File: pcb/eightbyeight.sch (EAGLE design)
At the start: 140 parts, among them CON1 USB_MICROSMT+THRUHULE, Q1 16MHz, SW1 SWITCH_SPDT, SW2 BRIGHTNESS, U1 MK20DN64VFM5, U10 FDG6316P, U11 FDG6316P, U12 FDG6316P, U2 ICN2026, U3 74138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

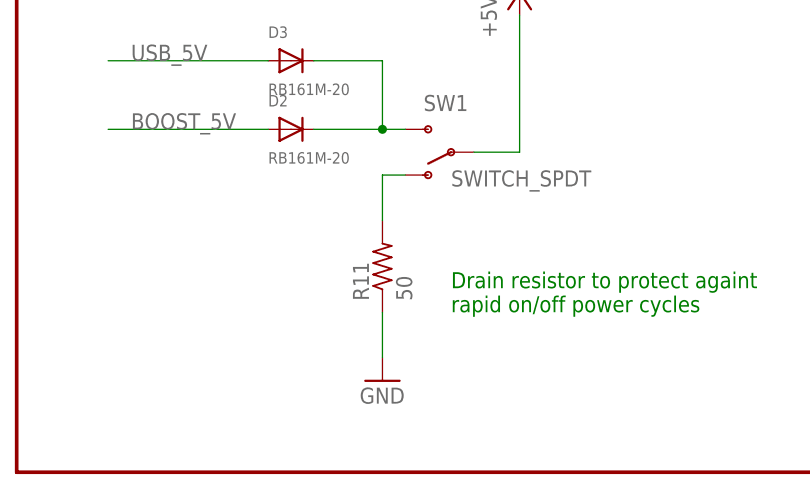
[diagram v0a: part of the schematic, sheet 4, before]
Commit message: Update board TODOs
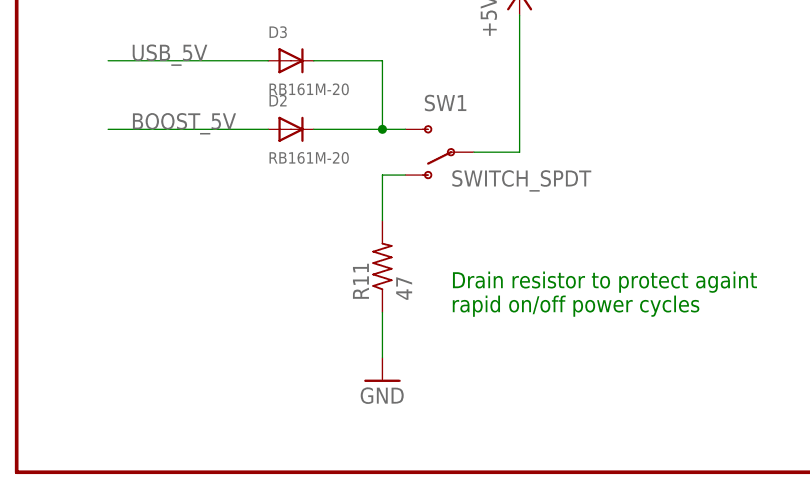
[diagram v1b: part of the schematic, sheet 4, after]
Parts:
- R11: value 50 -> 47
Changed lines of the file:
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@@
 <part name="D2" library="adafruit" deviceset="DIODE" device="SOD-123" value="RB161M-20"/>
 <part name="D3" library="adafruit" deviceset="DIODE" device="SOD-123" value="RB161M-20"/>
-<part name="R11" library="adafruit" deviceset="R-US_" device="R0805" value="50"/>
+<part name="R11" library="adafruit" deviceset="R-US_" device="R0805" value="47"/>
 <part name="GND43" library="SparkFun-Aesthetics" deviceset="GND" device=""/>
 <part name="16" library="testpad" deviceset="PTR1" device="B2,54"/>

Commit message: Silkscreen tweaks to pcbs
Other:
- note added: "High side (row) drivers"
- note removed: "High side (column) drivers"
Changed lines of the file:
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@@
 <wire x1="7.62" y1="101.6" x2="276.86" y2="101.6" width="0.4064" layer="94"/>
 <text x="12.7" y="71.12" size="1.778" layer="91">P channel MOSFETs with gate drive capability</text>
-<text x="12.7" y="76.2" size="2.54" layer="94">High side (column) drivers</text>
+<text x="12.7" y="76.2" size="2.54" layer="94">High side (row) drivers</text>
 <wire x1="7.62" y1="83.82" x2="274.32" y2="83.82" width="0.4064" layer="94"/>
 <wire x1="7.62" y1="7.62" x2="7.62" y2="83.82" width="0.4064" layer="94"/>

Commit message: Test pads in progress
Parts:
- removed U$2: JTAG_ARM_10PIN, blinkinlabs:JTAG_ARM_10PIN
- added R22: 100, adafruit:R-US_R0402
- added TP1, TP10, TP11, TP12, TP13, TP14, TP15, TP17, TP18, TP19, TP2, TP20, TP21, TP22, TP23, TP24, TP3, TP4, TP5, TP6, TP7, TP8, TP9: PTR1B1,27, testpad:PTR1B1,27
- C16: value 470pF -> 47pF
- D1: value BLUE -> ORANGE
- D4: value BLUE -> PURPLE
- R12, R23, R25, R26, R27, R6: value 10k -> 47k
- R21: value 2k 1% -> 47k
- R28: value 10k -> DNP
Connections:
- new net N$1: D1.C, D4.C, R22.2
- net +5V: now also TP7.TP
- net ARM_3V3: now also TP9.TP; no longer U$2.VCC
- net ARM_RESET: now also TP14.TP; no longer U$2.RESET
- net ARM_RX: now also TP13.TP; no longer U$2.TDI
- net ARM_RX1: now also TP23.TP
- net ARM_TCK: now also TP11.TP; no longer U$2.TCK
- net ARM_TMS: now also TP10.TP; no longer U$2.TMS
- net ARM_TX: now also TP12.TP; no longer U$2.TDO
- net BOOST_5V: now also TP24.TP
- net ESP_GPIO0: now also TP15.TP
- net ESP_RESET: now also TP17.TP
- net GND: now also R22.1, TP18.TP; no longer D1.C, D4.C, U$2.GND
- net I2C_SCL: now also TP6.TP
- net I2C_SDA: now also TP5.TP
- net LED_CLK: now also TP2.TP
- net LED_DAT_0: now also TP1.TP
- net LED_HS_EN: now also TP22.TP
- net LED_OE: now also TP4.TP
- net LED_ROW_A: now also TP19.TP
- net LED_ROW_B: now also TP20.TP
- net LED_ROW_C: now also TP21.TP
- net LED_STB: now also TP3.TP
- net VBAT: now also TP8.TP
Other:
- note added: "ESP test pins"
- note added: "JTAG interface for ARM"
- note added: "LED Test points"
- note added: "Momentary, active low Connected to ESP"
- note added: "Note: The I2C bus runs at 100KHz"
- note added: "Pin assignments for matrix output: LED_DAT + LED_CLK use ESPI hardware LED_OE needs to be on a pin with FTM capability LED_ROW_* and LED_STB are GPIO and need to be together on a unique port"
- note added: "Power supply Test points"
- note added: "Used during automated production testing Note: RX and TX are available on the ARM JTAG pins"
- note added: "Used for automated production testing"
- note removed: "ARM 10pin JTAG/SWD"
- note removed: "Momentary, active low Connected to ESP and ARM"
- note removed: "Note: Check that these values are correct for 3.3V"
- note removed: "Pin assignments for matrix output: LED_DAT + LED_CLK need to be together on a unique port LED_ROW_* and LED_STB need to be together on a unique port LED_OE needs to be on a pin with FTM capability"

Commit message: Closer to RevD
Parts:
- removed L2: 130ohm @100MHz, blinkinlabs:FB0805/NO-OUTLINE
- removed R22: 100, adafruit:R-US_R0402
- added SJ1: SOLDERJUMPERTRACE, SparkFun-Passives:SOLDERJUMPERTRACE
- added TP25: PTR1B1,27, testpad:PTR1B1,27
- added Z3: PGB1010603, PaxInstrument-T400:SPARKFUN-RESISTORS_RESISTOR0603-RES
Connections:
- removed net BUTTON1: R28.1, SW2.P, U6.IO4
- removed net SHIELD: CON1.SHIELD, L2.P$1
- new net BUTTON: R28.1, SW2.P, TP25.TP, U6.IO4
- net GND: now also CON1.SHIELD, SJ1.1, Z3.1; no longer L2.P$2, R22.1
- net N$1: now also SJ1.2; no longer R22.2
- net USB_5V: now also Z3.2
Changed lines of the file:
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@@
 <part name="GND6" library="SparkFun-Aesthetics" deviceset="GND" device=""/>
 <part name="GND1" library="supply1" deviceset="GND" device=""/>
-<part name="L2" library="blinkinlabs" deviceset="FB" device="0805/NO-OUTLINE" value="130ohm @100MHz"/>
 <part name="Q1" library="blinkinlabs" deviceset="CRYSTAL_4PAD" device="2520" value="16MHz"/>
 <part name="Z1" library="PaxInstrument-T400" deviceset="SPARKFUN-RESISTORS_RESISTOR" device="0603-RES" value="PGB1010603">
@@
 <part name="TP22" library="testpad" deviceset="PTR1" device="B1,27"/>
 <part name="GND20" library="SparkFun-Aesthetics" deviceset="GND" device=""/>
-<part name="R22" library="adafruit" deviceset="R-US_" device="R0402" value="100"/>
 <part name="TP23" library="testpad" deviceset="PTR1" device="B1,27"/>
 <part name="TP24" library="testpad" deviceset="PTR1" device="B1,27"/>
+<part name="TP25" library="testpad" deviceset="PTR1" device="B1,27"/>
+<part name="SJ1" library="SparkFun-Passives" deviceset="SOLDERJUMPER" device="TRACE"/>
+<part name="Z3" library="PaxInstrument-T400" deviceset="SPARKFUN-RESISTORS_RESISTOR" device="0603-RES" value="PGB1010603">
+<attribute name="MF" value="Littelfuse"/>
+<attribute name="MPN" value="PGB1010603NRHF"/>
+</part>
+<part name="GND45" library="supply1" deviceset="GND" device=""/>
+<part name="GND46" library="supply1" deviceset="GND" device=""/>
 </parts>
 <sheets>
@@
 -Update filter caps for 3.3V regulator
 -Add limiting resistor for status LEDs to make them less bright (TODO: Test me)
+-Add test pads for production
 TODO:
 -Implement more user friendly expansion pads for the ESP
 -Cosmetic: ESP8266 GPIO 18mislabeled, should be 16
 -Characterize the power situation
--test a flush-mount USB connector
--remove pullup resistor on button?
--Add test pads for production</text>
+-test a flush-mount USB connector</text>
 <text x="129.54" y="358.14" size="10.16" layer="91" align="bottom-center">EightByEight Blinky Badge</text>
 <text x="129.54" y="345.44" size="6.4516" layer="91" align="bottom-center">Copyright 2016 Blinkinlabs, LLC</text>
@@
 <attribute name="VALUE" x="76.962" y="50.546" size="1.778" layer="96"/>
 </instance>
-<instance part="GND7" gate="1" x="35.56" y="22.86"/>
+<instance part="GND7" gate="1" x="40.64" y="22.86"/>
 <instance part="CON1" gate="G$1" x="27.94" y="53.34"/>
 <instance part="C2" gate="G$1" x="30.48" y="215.9"/>
@@
 <instance part="C3" gate="G$1" x="43.18" y="215.9"/>
 <instance part="GND1" gate="1" x="55.88" y="22.86"/>
-<instance part="L2" gate="G$1" x="35.56" y="35.56" rot="R90"/>
 <instance part="Q1" gate="G$1" x="66.04" y="175.26"/>
 <instance part="Z1" gate="G$1" x="55.88" y="40.64" smashed="yes" rot="R90">
@@
 <instance part="TP18" gate="G$1" x="233.68" y="114.3" rot="R90"/>
 <instance part="GND22" gate="1" x="228.6" y="109.22"/>
+<instance part="Z3" gate="G$1" x="48.26" y="40.64" smashed="yes" rot="R90">
+<attribute name="VALUE" x="51.308" y="33.528" size="1.778" layer="96" rot="R90"/>
+<attribute name="MPN" x="48.26" y="40.64" size="1.778" layer="96" rot="R90" display="off"/>
+<attribute name="MF" x="48.26" y="40.64" size="1.778" layer="96" rot="R90" display="off"/>
+</instance>
+<instance part="GND45" gate="1" x="48.26" y="22.86"/>
+<instance part="GND46" gate="1" x="63.5" y="22.86"/>
 </instances>
 <busses>
@@
 </segment>
 <segment>
-<wire x1="63.5" y1="35.56" x2="63.5" y2="27.94" width="0.1524" layer="91"/>
-<wire x1="63.5" y1="27.94" x2="55.88" y2="27.94" width="0.1524" layer="91"/>
-<wire x1="55.88" y1="25.4" x2="55.88" y2="27.94" width="0.1524" layer="91"/>
+<pinref part="Z1" gate="G$1" pin="1"/>
 <pinref part="GND1" gate="1" pin="GND"/>
-<pinref part="Z1" gate="G$1" pin="1"/>
+<wire x1="55.88" y1="25.4" x2="55.88" y2="35.56" width="0.1524" layer="91"/>
+</segment>
+<segment>
+<wire x1="63.5" y1="35.56" x2="63.5" y2="25.4" width="0.1524" layer="91"/>
 <pinref part="Z2" gate="G$1" pin="1"/>
-<junction x="55.88" y="27.94"/>
-<wire x1="55.88" y1="27.94" x2="55.88" y2="35.56" width="0.1524" layer="91"/>
-</segment>
-<segment>
-<pinref part="L2" gate="G$1" pin="P$2"/>
+<pinref part="GND46" gate="1" pin="GND"/>
+</segment>
+<segment>
 <pinref part="GND7" gate="1" pin="GND"/>
-<wire x1="35.56" y1="30.48" x2="35.56" y2="27.94" width="0.1524" layer="91"/>
-<wire x1="35.56" y1="27.94" x2="35.56" y2="25.4" width="0.1524" layer="91"/>
 <pinref part="CON1" gate="G$1" pin="GND"/>
-<wire x1="43.18" y1="48.26" x2="35.56" y2="48.26" width="0.1524" layer="91"/>
-<wire x1="43.18" y1="48.26" x2="43.18" y2="27.94" width="0.1524" layer="91"/>
-<wire x1="43.18" y1="27.94" x2="35.56" y2="27.94" width="0.1524" layer="91"/>
-<junction x="35.56" y="27.94"/>
+<wire x1="40.64" y1="48.26" x2="35.56" y2="48.26" width="0.1524" layer="91"/>
+<wire x1="40.64" y1="48.26" x2="40.64" y2="43.18" width="0.1524" layer="91"/>
+<pinref part="CON1" gate="G$1" pin="SHIELD"/>
+<wire x1="40.64" y1="43.18" x2="40.64" y2="25.4" width="0.1524" layer="91"/>
+<wire x1="35.56" y1="43.18" x2="40.64" y2="43.18" width="0.1524" layer="91"/>
+<junction x="40.64" y="43.18"/>
 </segment>
 <segment>
@@
 <wire x1="228.6" y1="114.3" x2="228.6" y2="111.76" width="0.1524" layer="91"/>
 <pinref part="GND22" gate="1" pin="GND"/>
+</segment>
+<segment>
+<pinref part="Z3" gate="G$1" pin="1"/>
+<wire x1="48.26" y1="35.56" x2="48.26" y2="25.4" width="0.1524" layer="91"/>
+<pinref part="GND45" gate="1" pin="GND"/>
 </segment>
 </net>
@@
 </segment>
 </net>
-<net name="SHIELD" class="0">
-<segment>
-<pinref part="CON1" gate="G$1" pin="SHIELD"/>
-<pinref part="L2" gate="G$1" pin="P$1"/>
-<wire x1="35.56" y1="43.18" x2="35.56" y2="40.64" width="0.1524" layer="91"/>
-</segment>
-</net>
 <net name="ARM_TX" class="0">
 <segment>
@@
 <label x="50.8" y="58.42" size="1.778" layer="95"/>
 <pinref part="CON1" gate="G$1" pin="VCC"/>
-<wire x1="58.42" y1="58.42" x2="35.56" y2="58.42" width="0.1524" layer="91"/>
+<wire x1="58.42" y1="58.42" x2="48.26" y2="58.42" width="0.1524" layer="91"/>
+<pinref part="Z3" gate="G$1" pin="2"/>
+<wire x1="48.26" y1="58.42" x2="35.56" y2="58.42" width="0.1524" layer="91"/>
+<wire x1="48.26" y1="45.72" x2="48.26" y2="58.42" width="0.1524" layer="91"/>
+<junction x="48.26" y="58.42"/>
 </segment>
 </net>
@@
 <instance part="TP17" gate="G$1" x="307.34" y="137.16" rot="R90"/>
 <instance part="TP23" gate="G$1" x="307.34" y="121.92" rot="R90"/>
+<instance part="TP25" gate="G$1" x="307.34" y="116.84" rot="R90"/>
 </instances>
 <busses>
@@
 </segment>
 </net>
-<net name="BUTTON1" class="0">
+<net name="BUTTON" class="0">
 <segment>
 <label x="124.46" y="127" size="1.778" layer="95"/>
@@
 <wire x1="86.36" y1="215.9" x2="104.14" y2="215.9" width="0.1524" layer="91"/>
 <label x="91.44" y="215.9" size="1.778" layer="95"/>
+</segment>
+<segment>
+<pinref part="TP25" gate="G$1" pin="TP"/>
+<wire x1="304.8" y1="116.84" x2="289.56" y2="116.84" width="0.1524" layer="91"/>
+<label x="289.56" y="116.84" size="1.778" layer="95"/>
 </segment>
 </net>
@@
 <instance part="TP8" gate="G$1" x="299.72" y="223.52" rot="R90"/>
 <instance part="P+6" gate="1" x="292.1" y="233.68"/>
-<instance part="GND20" gate="1" x="116.84" y="170.18"/>
-<instance part="R22" gate="G$1" x="116.84" y="182.88" smashed="yes" rot="R90">
-<attribute name="NAME" x="115.8494" y="177.292" size="1.778" layer="95" rot="R90"/>
-<attribute name="VALUE" x="115.824" y="185.928" size="1.778" layer="96" rot="R90"/>
-</instance>
+<instance part="GND20" gate="1" x="127" y="170.18"/>
 <instance part="TP24" gate="G$1" x="299.72" y="218.44" rot="R90"/>
+<instance part="SJ1" gate="1" x="127" y="182.88" rot="R90"/>
 </instances>
 <busses>
@@
 <segment>
 <pinref part="GND20" gate="1" pin="GND"/>
-<pinref part="R22" gate="G$1" pin="1"/>
-<wire x1="116.84" y1="172.72" x2="116.84" y2="177.8" width="0.1524" layer="91"/>
+<pinref part="SJ1" gate="1" pin="1"/>
+<wire x1="127" y1="177.8" x2="127" y2="172.72" width="0.1524" layer="91"/>
 </segment>
 </net>
@@
 <pinref part="D1" gate="G$1" pin="C"/>
 <wire x1="127" y1="190.5" x2="127" y2="193.04" width="0.1524" layer="91"/>
-<pinref part="R22" gate="G$1" pin="2"/>
-<wire x1="116.84" y1="187.96" x2="116.84" y2="190.5" width="0.1524" layer="91"/>
-<junction x="116.84" y="190.5"/>
-</segment>
-</net>
+<pinref part="SJ1" gate="1" pin="2"/>
+<wire x1="127" y1="187.96" x2="127" y2="190.5" width="0.1524" layer="91"/>
+<junction x="127" y="190.5"/>
+</segment>
+</net>

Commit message: Final RevD
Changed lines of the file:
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@@
 -Change value of pullup resistors from 10k to 47k
 -Update filter caps for 3.3V regulator
--Add limiting resistor for status LEDs to make them less bright (TODO: Test me)
 -Add test pads for production
 TODO:

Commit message: Clean up board silkscreen
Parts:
- R1: value 2k 1% -> 1.8k 1%
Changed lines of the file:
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@@
 <part name="GND2" library="SparkFun-Aesthetics" deviceset="GND" device=""/>
 <part name="C7" library="adafruit" deviceset="C-US" device="C0402" value="100nF"/>
-<part name="R1" library="adafruit" deviceset="R-US_" device="R0402" value="2k 1%"/>
+<part name="R1" library="adafruit" deviceset="R-US_" device="R0402" value="1.8k 1%"/>
 <part name="GND3" library="SparkFun-Aesthetics" deviceset="GND" device=""/>
 <part name="GND4" library="SparkFun-Aesthetics" deviceset="GND" device=""/>
